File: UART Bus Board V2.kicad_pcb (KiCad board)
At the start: 4 copper layers, 55.9 x 27.9 mm, 63 parts, among them IC1 FT4232H-56Q-TRAY, J1 USB_B_Mini, J8 3.3V/5V GND TX RX TX RX TX RX, SW1 B3F-1000, U1 TC1262-33, U2 93AA46B, U3 MAX3232IPWR, U4 MAX3232IPWR, U5 M74HC595YTTR, Y1 ECS-120-8-30-JGN-TR

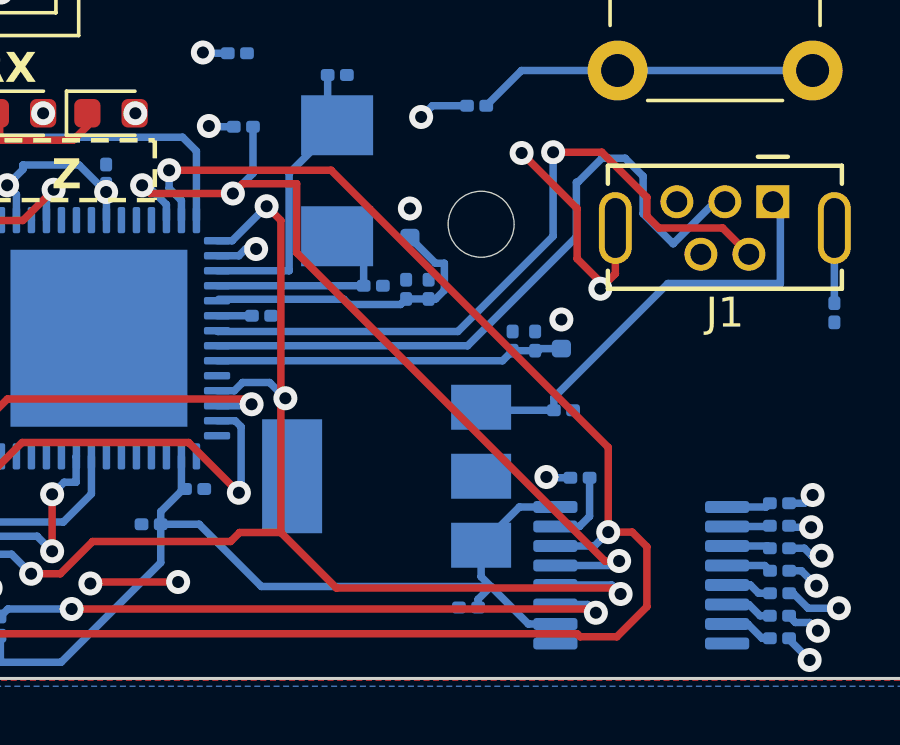
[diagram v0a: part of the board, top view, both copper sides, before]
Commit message: Errors & warning
Fixed a couple of errors and warnings that the DRC reported.
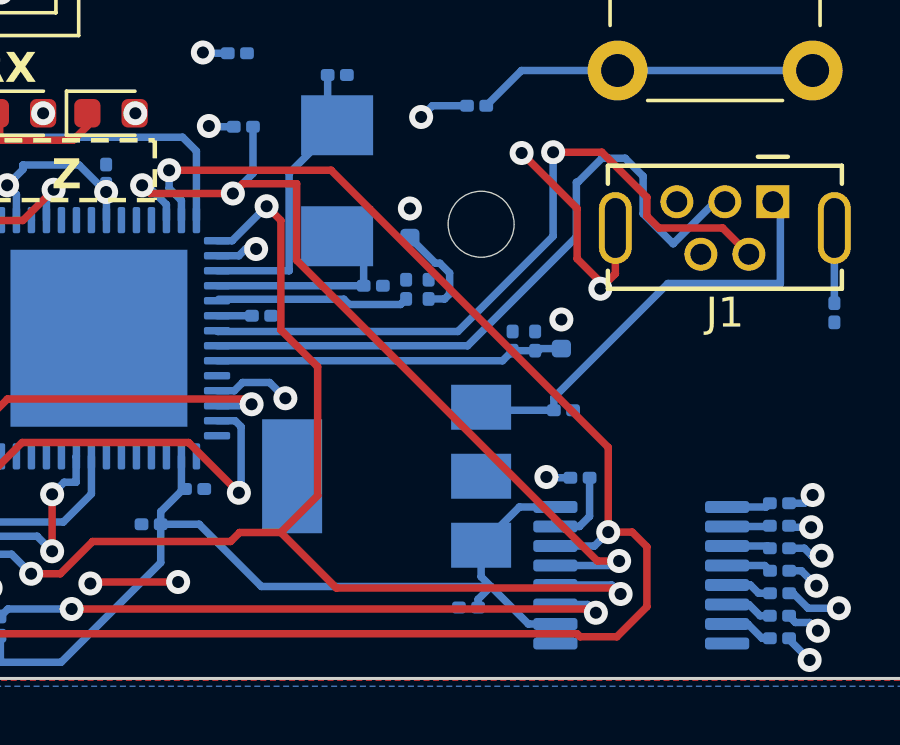
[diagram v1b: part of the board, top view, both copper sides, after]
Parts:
- removed REF** (x2): MountingHole_2.2mm_M2, MountingHole:MountingHole_2.2mm_M2
- added H1: MountingHole, MountingHole:MountingHole_2.2mm_M2, F.Cu at (131.2, 98.8)
- added H2: MountingHole, MountingHole:MountingHole_2.2mm_M2, F.Cu at (158.4, 98.8)
- turned C7 to 90 degrees
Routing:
- net Net-(IC1-EECS): track 41.0 -> 42.0 mm
- net Net-(IC1-VPHY): track 10.2 -> 9.68 mm

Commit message: clearances/minimums + burried vias + PCBWay
Lowered clearances and minimums on the top fill layer
Removed three buried/hidden vias
Passing on PCBWay without issues
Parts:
- C1, C4: value 100 nF -> 1 uF
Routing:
- net +3.3V: track 46.4 -> 48.8 mm
- net Net-(D3-A): track 48.2 -> 50.4 mm
- net Net-(D4-A): track 47.4 -> 49.5 mm
- net Net-(D6-A): track 72.1 -> 73.7 mm
- net Net-(D7-A): track 70.6 -> 72.1 mm
- net Net-(D1-A): track 44.6 -> 46.0 mm
- net Net-(D2-A): track 52.9 -> 54.2 mm
- net Net-(D5-A): track 75.3 -> 76.4 mm
- net Net-(IC1-VPHY): track 9.68 -> 10.4 mm
